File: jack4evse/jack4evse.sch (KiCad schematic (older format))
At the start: 10 parts, among them J1 Conn_02x08_Odd_Even, J2 Conn_01x04, J3 Conn_01x04, J4 Conn_02x08_Odd_Even, J5 Conn_01x04, J6 Conn_01x04

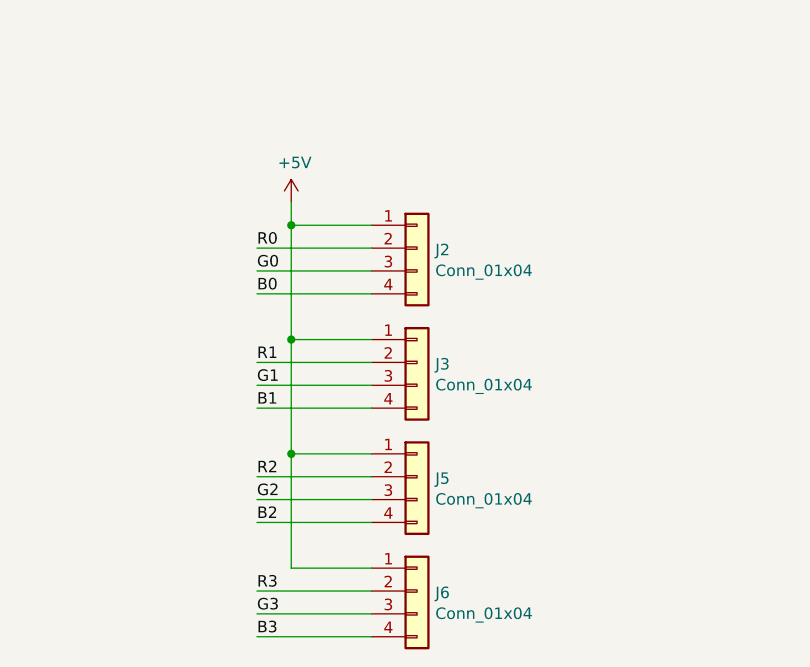
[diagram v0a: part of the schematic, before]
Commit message: jack/sch: Switch main headers to 1x16
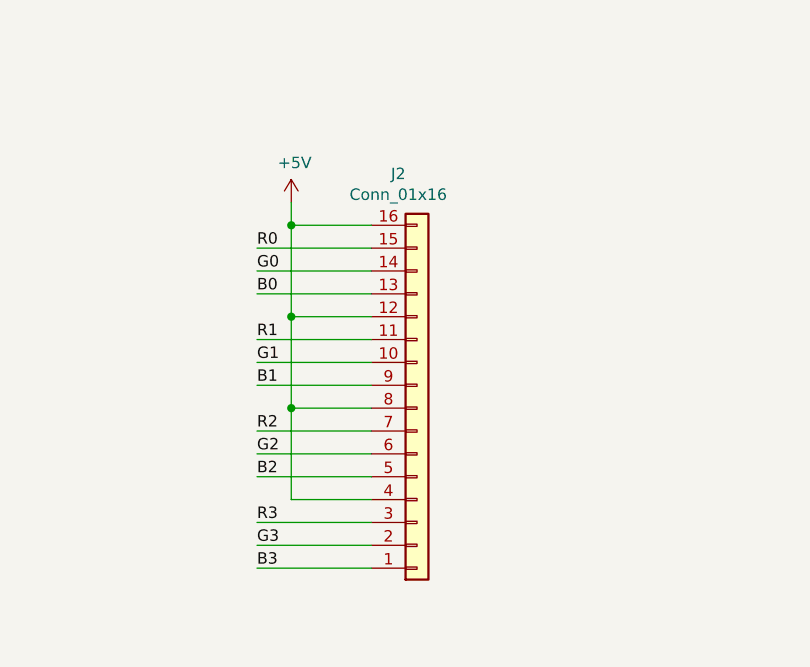
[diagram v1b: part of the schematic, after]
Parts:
- removed J2, J3, J5, J6: Conn_01x04, Connector_PinHeader_2.54mm:PinHeader_1x04_P2.54mm_Horizontal, symbol Connector_Generic:Conn_01x04
- added J2: Conn_01x16, Connector_PinHeader_2.54mm:PinHeader_1x16_P2.54mm_Horizontal, symbol Connector_Generic:Conn_01x16
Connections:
- net +5V: now also J2.12 (Pin_12), J2.16 (Pin_16), J2.4 (Pin_4), J2.8 (Pin_8)
- net B0: now also J2.13 (Pin_13)
- net B1: now also J2.9 (Pin_9)
- net B2: now also J2.5 (Pin_5)
- net B3: now also J2.1 (Pin_1)
- net G0: now also J2.14 (Pin_14)
- net G1: now also J2.10 (Pin_10)
- net G2: now also J2.6 (Pin_6)
- net G3: now also J2.2 (Pin_2)
- net R0: now also J2.15 (Pin_15)
- net R1: now also J2.11 (Pin_11)
- net R2: now also J2.7 (Pin_7)
- net R3: now also J2.3 (Pin_3)
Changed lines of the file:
@@
 	4600 4100 4950 4100
+Wire Wire Line
+	4950 4600 4450 4600
+Text Label 4450 4600 0    50   ~ 0
+R1
 Wire Wire Line
 	4950 4700 4450 4700
 Text Label 4450 4700 0    50   ~ 0
-R1
+G1
 Wire Wire Line
 	4950 4800 4450 4800
 Text Label 4450 4800 0    50   ~ 0
-G1
-Wire Wire Line
-	4950 4900 4450 4900
-Text Label 4450 4900 0    50   ~ 0
 B1
 Wire Wire Line
-	4600 4600 4950 4600
+	4600 4500 4950 4500
+Wire Wire Line
+	4950 5000 4450 5000
+Text Label 4450 5000 0    50   ~ 0
+R2
+Wire Wire Line
+	4950 5100 4450 5100
+Text Label 4450 5100 0    50   ~ 0
+G2
 Wire Wire Line
 	4950 5200 4450 5200
 Text Label 4450 5200 0    50   ~ 0
-R2
-Wire Wire Line
-	4950 5300 4450 5300
-Text Label 4450 5300 0    50   ~ 0
-G2
+B2
+Wire Wire Line
+	4600 4900 4950 4900
 Wire Wire Line
 	4950 5400 4450 5400
 Text Label 4450 5400 0    50   ~ 0
-B2
-Wire Wire Line
-	4600 5100 4950 5100
-Wire Wire Line
-	4950 5700 4450 5700
-Text Label 4450 5700 0    50   ~ 0
 R3
 Wire Wire Line
-	4950 5800 4450 5800
-Text Label 4450 5800 0    50   ~ 0
+	4950 5500 4450 5500
+Text Label 4450 5500 0    50   ~ 0
 G3
 Wire Wire Line
-	4950 5900 4450 5900
-Text Label 4450 5900 0    50   ~ 0
+	4950 5600 4450 5600
+Text Label 4450 5600 0    50   ~ 0
 B3
 Wire Wire Line
-	4600 5600 4950 5600
+	4600 5300 4950 5300
 $Comp
 L Connector_Generic:Conn_02x08_Odd_Even J1
@@
 Output\n
 $Comp
-L Connector_Generic:Conn_01x04 J2
-U 1 1 5DD0F963
-P 5150 4200
-F 0 "J2" H 5230 4192 50  0000 L CNN
-F 1 "Conn_01x04" H 5230 4101 50  0000 L CNN
-F 2 "Connector_PinHeader_2.54mm:PinHeader_1x04_P2.54mm_Horizontal" H 5150 4200 50  0001 C CNN
-F 3 "~" H 5150 4200 50  0001 C CNN
-	1    5150 4200
-	1    0    0    -1
-$EndComp
-$Comp
-L Connector_Generic:Conn_01x04 J3
-U 1 1 5DD151CE
-P 5150 4700
-F 0 "J3" H 5230 4692 50  0000 L CNN
-F 1 "Conn_01x04" H 5230 4601 50  0000 L CNN
-F 2 "Connector_PinHeader_2.54mm:PinHeader_1x04_P2.54mm_Horizontal" H 5150 4700 50  0001 C CNN
-F 3 "~" H 5150 4700 50  0001 C CNN
-	1    5150 4700
-	1    0    0    -1
-$EndComp
-$Comp
-L Connector_Generic:Conn_01x04 J5
-U 1 1 5DD17FE5
-P 5150 5200
-F 0 "J5" H 5230 5192 50  0000 L CNN
-F 1 "Conn_01x04" H 5230 5101 50  0000 L CNN
-F 2 "Connector_PinHeader_2.54mm:PinHeader_1x04_P2.54mm_Horizontal" H 5150 5200 50  0001 C CNN
-F 3 "~" H 5150 5200 50  0001 C CNN
-	1    5150 5200
-	1    0    0    -1
-$EndComp
-$Comp
-L Connector_Generic:Conn_01x04 J6
-U 1 1 5DD1860C
-P 5150 5700
-F 0 "J6" H 5230 5692 50  0000 L CNN
-F 1 "Conn_01x04" H 5230 5601 50  0000 L CNN
-F 2 "Connector_PinHeader_2.54mm:PinHeader_1x04_P2.54mm_Horizontal" H 5150 5700 50  0001 C CNN
-F 3 "~" H 5150 5700 50  0001 C CNN
-	1    5150 5700
-	1    0    0    -1
-$EndComp
-Wire Wire Line
-	4600 4100 4600 4600
-Connection ~ 4600 4100
-Wire Wire Line
-	4600 5100 4600 4600
-Connection ~ 4600 4600
-Wire Wire Line
-	4600 5100 4600 5600
-Connection ~ 4600 5100
-$Comp
 L power:+5V #PWR0101
 U 1 1 5DD2D382
@@
 Wire Wire Line
 	6150 3000 7100 3000
+$Comp
+L Connector_Generic:Conn_01x16 J2
+U 1 1 5DD5AF38
+P 5150 4900
+F 0 "J2" H 5068 3875 50  0000 C CNN
+F 1 "Conn_01x16" H 5068 3966 50  0000 C CNN
+F 2 "Connector_PinHeader_2.54mm:PinHeader_1x16_P2.54mm_Horizontal" H 5150 4900 50  0001 C CNN
+F 3 "~" H 5150 4900 50  0001 C CNN
+	1    5150 4900
+	1    0    0    1
+$EndComp
+Wire Wire Line
+	4600 4100 4600 4500
+Connection ~ 4600 4100
+Wire Wire Line
+	4600 4500 4600 4900
+Connection ~ 4600 4500
+Wire Wire Line
+	4600 4900 4600 5300
+Connection ~ 4600 4900
 $EndSCHEMATC

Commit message: jack: Change LED footprint to ma ones
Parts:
- D1, D2, D3, D4: footprint LED_SMD:LED_Avago_PLCC4_3.2x2.8mm_CW -> ma4evse:LED_Avago_PLCC4_3.2x2.8mm_CW
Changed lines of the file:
@@
 F 0 "D1" H 4050 2867 50  0000 C CNN
 F 1 "ASMB-MTB0-0A3A2" H 4050 2776 50  0000 C CNN
-F 2 "LED_SMD:LED_Avago_PLCC4_3.2x2.8mm_CW" H 4050 2850 50  0001 C CNN
+F 2 "ma4evse:LED_Avago_PLCC4_3.2x2.8mm_CW" H 4050 2850 50  0001 C CNN
 F 3 "https://docs.broadcom.com/docs/AV02-4186EN" H 4050 1900 50  0001 C CNN
 	1    4050 2350
@@
 F 0 "D2" H 5000 2867 50  0000 C CNN
 F 1 "ASMB-MTB0-0A3A2" H 5000 2776 50  0000 C CNN
-F 2 "LED_SMD:LED_Avago_PLCC4_3.2x2.8mm_CW" H 5000 2850 50  0001 C CNN
+F 2 "ma4evse:LED_Avago_PLCC4_3.2x2.8mm_CW" H 5000 2850 50  0001 C CNN
 F 3 "https://docs.broadcom.com/docs/AV02-4186EN" H 5000 1900 50  0001 C CNN
 	1    5000 2350
@@
 F 0 "D3" H 5950 2867 50  0000 C CNN
 F 1 "ASMB-MTB0-0A3A2" H 5950 2776 50  0000 C CNN
-F 2 "LED_SMD:LED_Avago_PLCC4_3.2x2.8mm_CW" H 5950 2850 50  0001 C CNN
+F 2 "ma4evse:LED_Avago_PLCC4_3.2x2.8mm_CW" H 5950 2850 50  0001 C CNN
 F 3 "https://docs.broadcom.com/docs/AV02-4186EN" H 5950 1900 50  0001 C CNN
 	1    5950 2350
@@
 F 0 "D4" H 6900 2867 50  0000 C CNN
 F 1 "ASMB-MTB0-0A3A2" H 6900 2776 50  0000 C CNN
-F 2 "LED_SMD:LED_Avago_PLCC4_3.2x2.8mm_CW" H 6900 2850 50  0001 C CNN
+F 2 "ma4evse:LED_Avago_PLCC4_3.2x2.8mm_CW" H 6900 2850 50  0001 C CNN
 F 3 "https://docs.broadcom.com/docs/AV02-4186EN" H 6900 1900 50  0001 C CNN
 	1    6900 2350

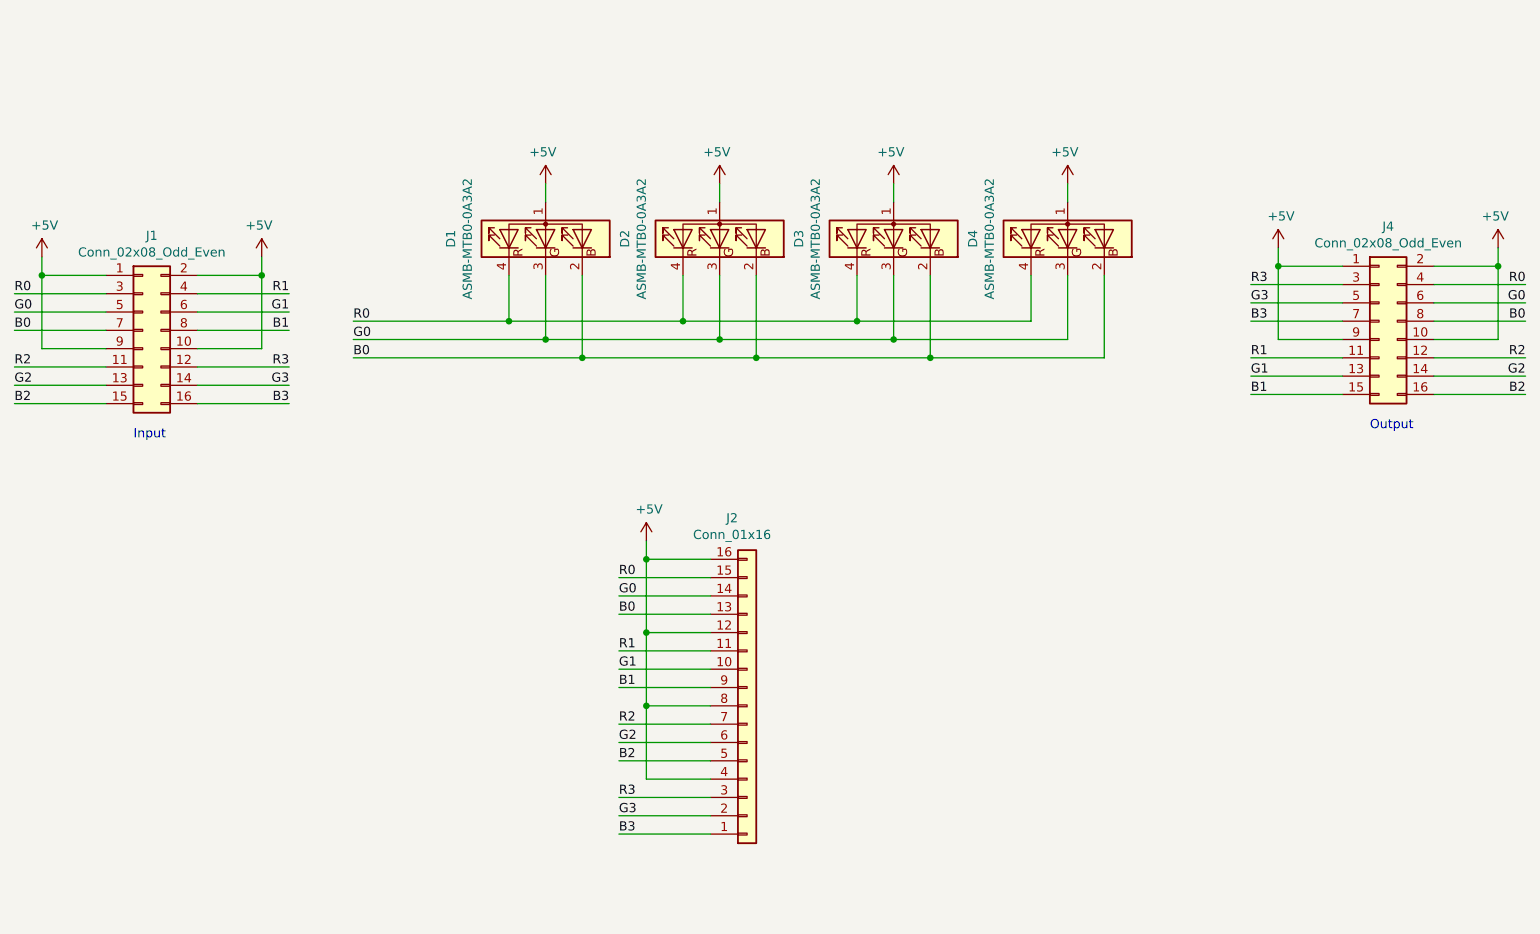
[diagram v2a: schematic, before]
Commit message: jack/{sch, pcb}: Make one single ring pcb with all leds
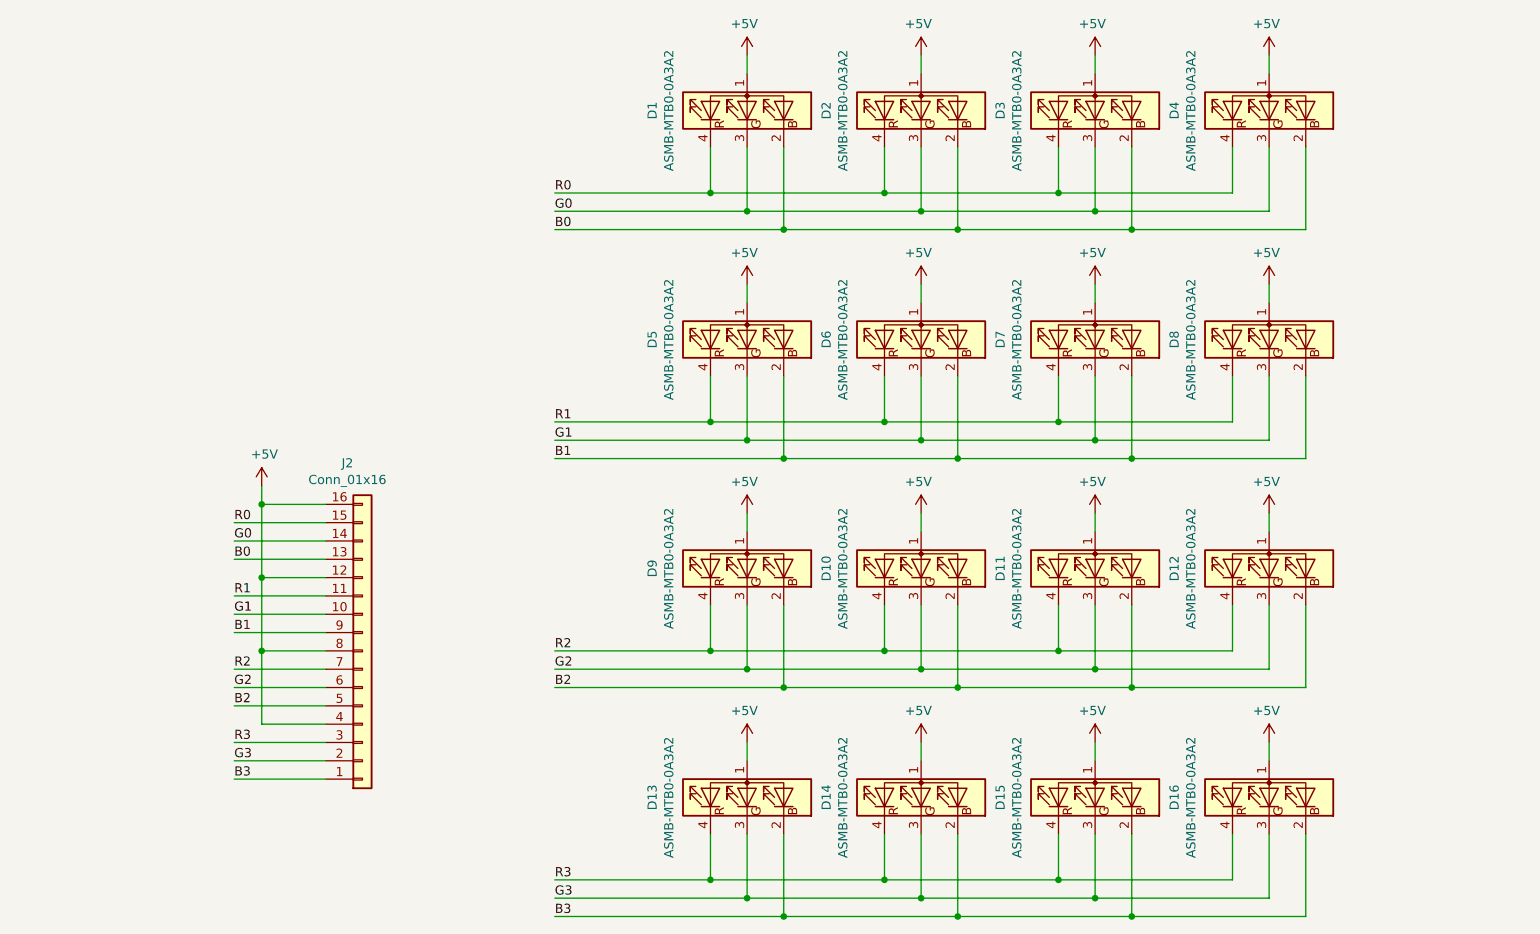
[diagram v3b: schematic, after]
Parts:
- removed J1: Conn_02x08_Odd_Even, ma4evse:CLP-108-02-F-DH, symbol Connector_Generic:Conn_02x08_Odd_Even
- removed J4: Conn_02x08_Odd_Even, ma4evse:PinHeader_2x08_P1.27mm_Horizontal, symbol Connector_Generic:Conn_02x08_Odd_Even
- added D10, D11, D12, D13, D14, D15, D16, D5, D6, D7, D8, D9: ASMB-MTB0-0A3A2, ma4evse:LED_Avago_PLCC4_3.2x2.8mm_CW, symbol LED:ASMB-MTB0-0A3A2
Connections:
- net +5V: now also D10.1 (A), D11.1 (A), D12.1 (A), D13.1 (A), D14.1 (A), D15.1 (A), D16.1 (A), D5.1 (A), D6.1 (A), D7.1 (A), D8.1 (A), D9.1 (A)
- net B1: now also D5.2 (BK), D6.2 (BK), D7.2 (BK), D8.2 (BK)
- net B2: now also D10.2 (BK), D11.2 (BK), D12.2 (BK), D9.2 (BK)
- net B3: now also D13.2 (BK), D14.2 (BK), D15.2 (BK), D16.2 (BK)
- net G1: now also D5.3 (GK), D6.3 (GK), D7.3 (GK), D8.3 (GK)
- net G2: now also D10.3 (GK), D11.3 (GK), D12.3 (GK), D9.3 (GK)
- net G3: now also D13.3 (GK), D14.3 (GK), D15.3 (GK), D16.3 (GK)
- net R1: now also D5.4 (RK), D6.4 (RK), D7.4 (RK), D8.4 (RK)
- net R2: now also D10.4 (RK), D11.4 (RK), D12.4 (RK), D9.4 (RK)
- net R3: now also D13.4 (RK), D14.4 (RK), D15.4 (RK), D16.4 (RK)
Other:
- note removed: "Input\n"
- note removed: "Output\n"
- moved on the sheet: D1, D2, D3, D4, J2
